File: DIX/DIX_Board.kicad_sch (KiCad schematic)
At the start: 16 parts

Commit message: More! Stuff!
Started on the actual board. Lots to learn.
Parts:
- removed C? (x3): 100n, symbol Device:C
- removed C?: 10u, symbol Device:C
- added C10, C5, C8: 10u, Capacitor_SMD:C_0805_2012Metric, symbol Device:C
- added C11, C7, C9: 100n, Capacitor_SMD:C_0805_2012Metric, symbol Device:C
- added C3, C4: 0.1u, Capacitor_SMD:C_0805_2012Metric_Pad1.18x1.45mm_HandSolder, symbol Device:C
- added C6: .1u, Capacitor_SMD:C_0805_2012Metric, symbol Device:C
- added IC1, IC2: TORX1950A_F_, TORX1950AF, symbol TORX1950A_F_:TORX1950A_F_
- added L1, L2: 47u, Inductor_SMD:L_0805_2012Metric_Pad1.05x1.20mm_HandSolder, symbol Device:L
- added R10, R11, R4, R5, R6, R7, R8, R9: 100, Resistor_SMD:R_0805_2012Metric_Pad1.20x1.40mm_HandSolder, symbol Device:R
- added R2: R, Resistor_SMD:R_0805_2012Metric_Pad1.20x1.40mm_HandSolder, symbol Device:R
- added R3: 10k, Resistor_SMD:R_0805_2012Metric_Pad1.20x1.40mm_HandSolder, symbol Device:R
- C1, C2: renamed from C?; value C -> 100u; footprint (none) -> Capacitor_SMD:C_0805_2012Metric_Pad1.18x1.45mm_HandSolder
- C12: renamed from C?; value C -> 0.1u; footprint (none) -> Capacitor_SMD:C_0805_2012Metric
- C13: renamed from C?; value C -> 0.01u; footprint (none) -> Capacitor_SMD:C_0805_2012Metric
- C14: renamed from C?; value C -> 2.2u; footprint (none) -> Capacitor_SMD:C_0805_2012Metric
- D1: renamed from D?; footprint (none) -> LED_THT:LED_D8.0mm
- J1, J2: renamed from J?; footprint (none) -> Connector_PinHeader_1.27mm:PinHeader_1x12_P1.27mm_Vertical
- R1: renamed from R?; value R -> 1k; footprint (none) -> Resistor_SMD:R_0805_2012Metric_Pad1.20x1.40mm_HandSolder
- gave numbers to parts that had none: 3
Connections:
- net +3.3V: now also C10.1, C11.1, C5.1, C7.1, C8.1, C9.1, R2.1, R3.1; no longer U2.9 (VCC)
- net GND: now also C6.1, IC1.MH1 (CASE_1), IC1.MH2 (CASE_2), IC2.MH1 (CASE_1), IC2.MH2 (CASE_2); no longer U2.44 (BGND)
- net at U2.1 (RX1+): now also IC1.1 (OUTPUT)
- net at U2.23 (*INT): now also R3.2
- net at U2.3 (RX2+): now also IC2.1 (OUTPUT)
- net at U2.37 (BCKA): now also R11.1
- net at U2.38 (LRCKA): now also R9.1
- net at U2.39 (SDINA): now also R7.1
- net at U2.40 (SDOUTA): now also R5.1
- net at U2.45 (SDOUTB): now also R10.1
- net at U2.46 (SDINB): now also R8.1
- net at U2.47 (LRCKB): now also R6.1
- net at U2.48 (BCKB): now also R4.1
- net 1V8 renamed +1V8
- net +1V8: now also C6.2
- new net: C10.2, C11.2
- new net: C3.2, IC1.2 (GND1), IC1.4 (GND2)
- new net: C3.1, IC1.3 (VCC), L1.2
- new net: C8.2, C9.2
- new net: C4.2, IC2.2 (GND1), IC2.4 (GND2)
- new net: C4.1, IC2.3 (VCC), L2.2
- new net: C5.2, C7.2
- new net: R2.2, U2.9 (VCC)
- new net +5V: L1.1, L2.1
- new net BCKA: R5.2
- new net BCKB: R4.2
- new net LRCKA: R7.2
- new net LRCKB: R6.2
- new net SDINA: R9.2
- new net SDINB: R8.2
- new net SDOUTA: R11.2
- new net SDOUTB: R10.2
- no-connect marks 0 -> 7
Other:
- note added: "Pull Up Resistor"

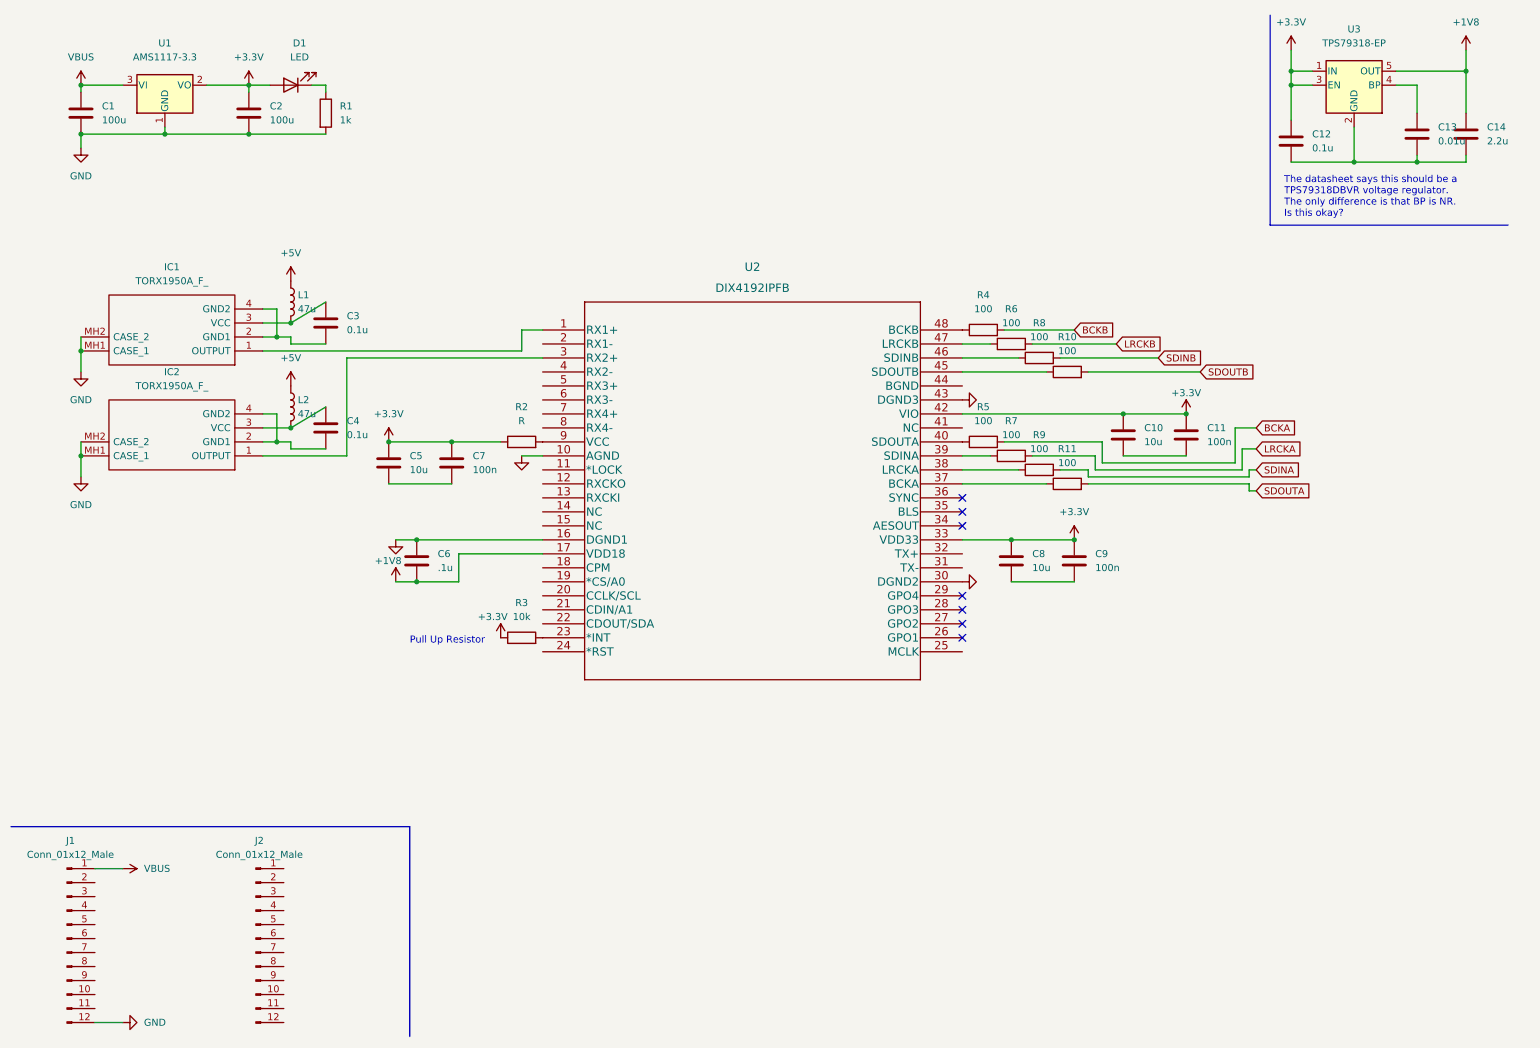
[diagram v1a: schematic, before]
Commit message: Less electrical check failures
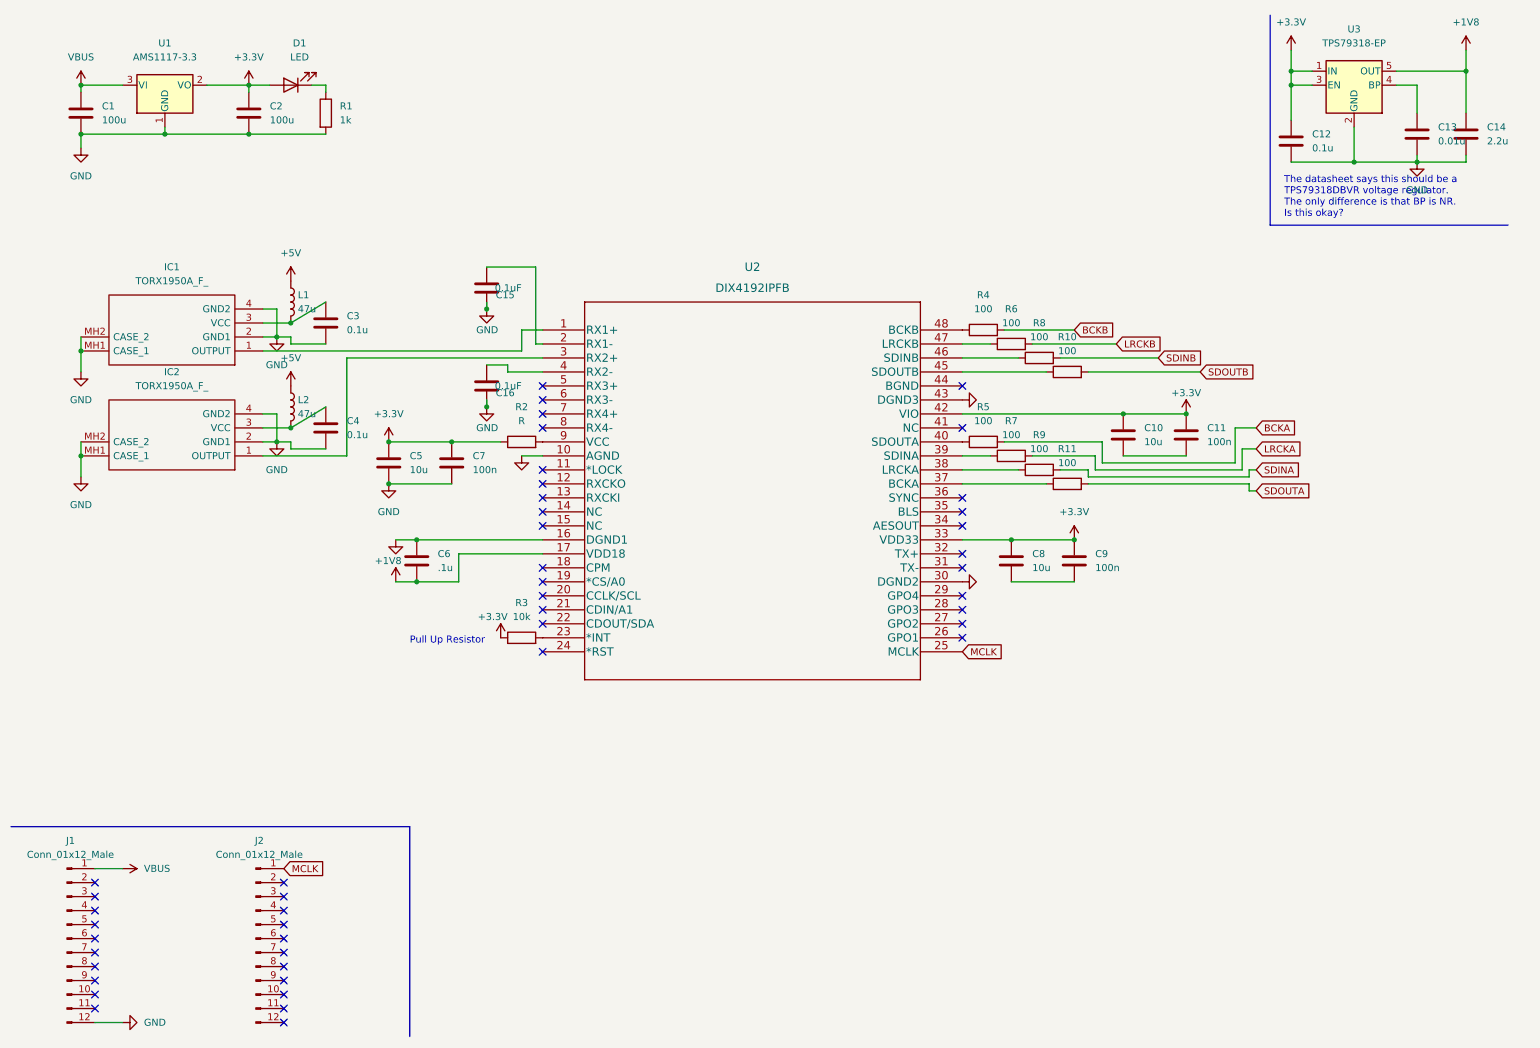
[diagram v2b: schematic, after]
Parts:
- added C15, C16: 0.1uF, Capacitor_SMD:C_0603_1608Metric_Pad1.08x0.95mm_HandSolder, symbol Device:C
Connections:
- net GND: now also C12.2, C13.2, C14.2, C3.2, C4.2, C5.2, C7.2, IC1.2 (GND1), IC1.4 (GND2), IC2.2 (GND1), IC2.4 (GND2), U3.2 (GND), C15.1, C16.1
- net MCLK: now reaches J2.1 (Pin_1)
- net MCLK: now also U2.25 (MCLK)
- net at U2.2 (RX1-): now also C15.2
- net at U2.4 (RX2-): now also C16.2
- no-connect marks 7 -> 47

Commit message: Some routing
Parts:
- IC1, IC2: footprint TORX1950AF -> Audio_Module:Reverb_BTDR-1H
- U2: footprint PFB48 -> DIX Footprints:DIX4192IPFB
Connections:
- net +5V: now also J2.1 (Pin_1)
- net BCKA: now also J1.3 (Pin_3)
- net BCKB: now also J1.7 (Pin_7)
- net GND: now also U2.44 (BGND)
- net LRCKA: now also J1.4 (Pin_4)
- net LRCKB: now also J1.8 (Pin_8)
- net MCLK: now also J1.2 (Pin_2); no longer J2.1 (Pin_1)
- net SDINA: now also J1.5 (Pin_5)
- net SDINB: now also J1.9 (Pin_9)
- net SDOUTA: now also J1.6 (Pin_6)
- net SDOUTB: now also J1.10 (Pin_10)
- net CCLK/SCL: now reaches J2.10 (Pin_10)
- net CCLK/SCL: now also U2.20 (CCLK/SCL)
- net *CS/AO: now reaches J2.11 (Pin_11)
- net *CS/AO: now also U2.19 (*CS/A0)
- net CPM: now reaches J2.12 (Pin_12)
- net CPM: now also U2.18 (CPM)
- net TX+: now reaches J2.2 (Pin_2)
- net TX+: now also U2.32 (TX+)
- net TX-: now reaches J2.3 (Pin_3)
- net TX-: now also U2.31 (TX-)
- net GPO4: now reaches J2.4 (Pin_4)
- net GPO4: now also U2.29 (GPO4)
- net GPO3: now reaches J2.5 (Pin_5)
- net GPO3: now also U2.28 (GPO3)
- net GPO2: now reaches J2.6 (Pin_6)
- net GPO2: now also U2.27 (GPO2)
- net GPO1: now reaches J2.7 (Pin_7)
- net GPO1: now also U2.26 (GPO1)
- net CDOUT/SDA: now reaches J2.8 (Pin_8)
- net CDOUT/SDA: now also U2.22 (CDOUT/SDA)
- net CDIN/A1: now reaches J2.9 (Pin_9)
- net CDIN/A1: now also U2.21 (CDIN/A1)
- no-connect marks 47 -> 15
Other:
- moved on the sheet: C16
